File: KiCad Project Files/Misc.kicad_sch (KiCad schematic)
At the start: 19 parts, among them J2 SWD, U5 74AHCT1G125

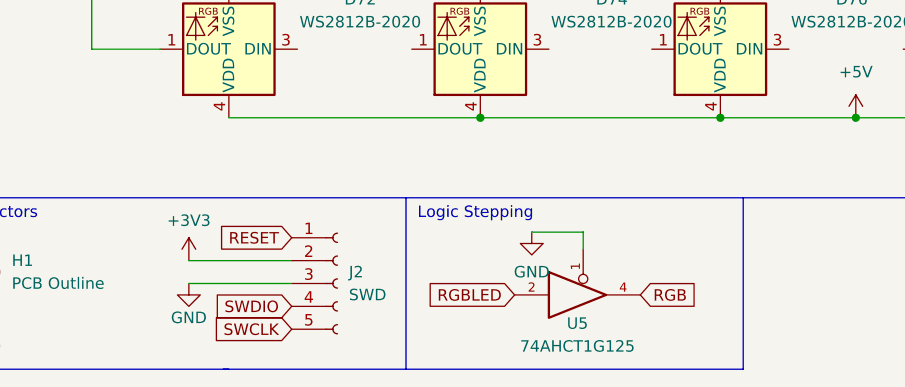
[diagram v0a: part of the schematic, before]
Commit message: begin work on stm32 branch
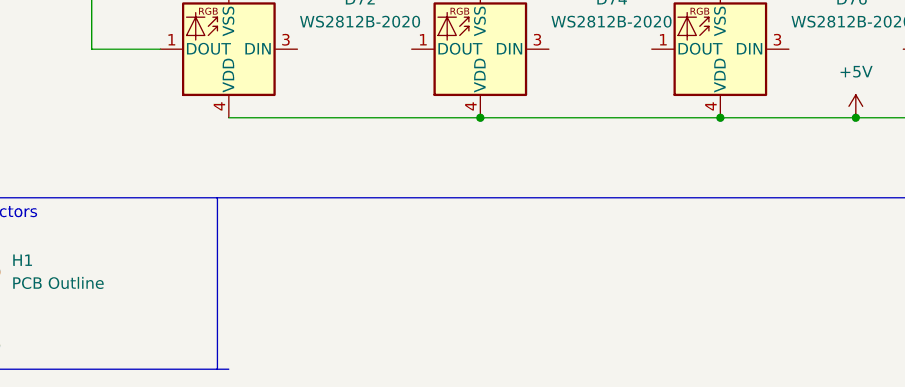
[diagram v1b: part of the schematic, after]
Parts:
- removed J2: SWD, Connector_PinHeader_2.54mm:PinHeader_1x05_P2.54mm_Vertical, symbol Connector:Conn_01x05_Female
- removed U5: 74AHCT1G125, Package_TO_SOT_SMD:SOT-23-5, symbol 74xGxx:74AHCT1G125
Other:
- note removed: "Logic Stepping"
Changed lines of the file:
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@@
-    (stroke (width 0) (type default) (color 0 0 0 0))
-  )
-  (wire (pts (xy 40.005 104.775) (xy 51.435 104.775))
     (stroke (width 0) (type default) (color 0 0 0 0))
   )
@@
     (stroke (width 0) (type default) (color 0 0 0 0))
   )
-  (polyline (pts (xy 101.6 114.3) (xy 101.6 95.25))
-    (stroke (width 0) (type default) (color 0 0 0 0))
-  )
-  (polyline (pts (xy 64.135 114.3) (xy 101.6 114.3))
-    (stroke (width 0) (type default) (color 0 0 0 0))
-  )
-  (wire (pts (xy 78.105 99.06) (xy 83.82 99.06))
+  (polyline (pts (xy 43.18 95.25) (xy 43.18 114.3))
     (stroke (width 0) (type default) (color 0 0 0 0))
   )
@@
     (stroke (width 0) (type default) (color 0 0 0 0))
   )
-  (wire (pts (xy 40.005 102.235) (xy 51.435 102.235))
-    (stroke (width 0) (type default) (color 0 0 0 0))
-  )
   (wire (pts (xy 44.45 19.685) (xy 71.755 19.685))
     (stroke (width 0) (type default) (color 0 0 0 0))
@@
     (stroke (width 0) (type default) (color 0 0 0 0))
   )
-  (polyline (pts (xy 43.815 114.3) (xy 64.135 114.3))
-    (stroke (width 0) (type default) (color 0 0 0 0))
-  )
-  (polyline (pts (xy 64.135 95.25) (xy 64.135 114.3))
-    (stroke (width 0) (type default) (color 0 0 0 0))
-  )
   (wire (pts (xy 133.985 27.305) (xy 146.05 27.305))
     (stroke (width 0) (type default) (color 0 0 0 0))
@@
     (stroke (width 0) (type default) (color 0 0 0 0))
   )
-  (wire (pts (xy 83.82 99.06) (xy 83.82 100.965))
-    (stroke (width 0) (type default) (color 0 0 0 0))
-  )
   (wire (pts (xy 71.755 19.685) (xy 99.06 19.685))
     (stroke (width 0) (type default) (color 0 0 0 0))
@@
   (polyline (pts (xy 222.25 95.25) (xy 12.7 95.25))
     (stroke (width 0) (type default) (color 0 0 0 0))
-  )
-  (text "Logic Stepping" (at 65.405 97.79 0)
-    (effects (font (size 1.27 1.27)) (justify left bottom))
   )
   (text "Connectors\n" (at 13.335 97.79 0)
@@
   (text "RGB\n" (at 13.335 15.24 0)
     (effects (font (size 1.27 1.27)) (justify left bottom))
-  )
-  (global_label "RGB" (shape input) (at 90.17 106.045 0) (fields_autoplaced)
-    (effects (font (size 1.27 1.27)) (justify left))
-    (property "Intersheet References" "${INTERSHEET_REFS}" (id 0) (at 96.3931 106.1244 0)
-      (effects (font (size 1.27 1.27)) (justify left) hide)
-    )
   )
   (global_label "RGB" (shape input) (at 36.83 27.305 180) (fields_autoplaced)
@@
     )
   )
-  (global_label "SWCLK" (shape input) (at 51.435 109.855 180) (fields_autoplaced)
-    (effects (font (size 1.27 1.27)) (justify right))
-    (property "Intersheet References" "${INTERSHEET_REFS}" (id 0) (at 42.7929 109.7756 0)
-      (effects (font (size 1.27 1.27)) (justify right) hide)
-    )
-  )
-  (global_label "RGBLED" (shape input) (at 76.2 106.045 180) (fields_autoplaced)
-    (effects (font (size 1.27 1.27)) (justify right))
-    (property "Intersheet References" "${INTERSHEET_REFS}" (id 0) (at 66.5298 105.9656 0)
-      (effects (font (size 1.27 1.27)) (justify right) hide)
-    )
-  )
-  (global_label "RESET" (shape input) (at 51.435 99.695 180) (fields_autoplaced)
-    (effects (font (size 1.27 1.27)) (justify right))
-    (property "Intersheet References" "${INTERSHEET_REFS}" (id 0) (at 43.2767 99.6156 0)
-      (effects (font (size 1.27 1.27)) (justify right) hide)
-    )
-  )
-  (global_label "SWDIO" (shape input) (at 51.435 107.315 180) (fields_autoplaced)
-    (effects (font (size 1.27 1.27)) (justify right))
-    (property "Intersheet References" "${INTERSHEET_REFS}" (id 0) (at 43.1557 107.2356 0)
-      (effects (font (size 1.27 1.27)) (justify right) hide)
-    )
-  )
   (symbol (lib_id "cipulot_parts:SK6812MINI") (at 29.21 43.18 90) (unit 1)
     (in_bom yes) (on_board yes) (fields_autoplaced)
@@
     (pin "4")
   )
-  (symbol (lib_id "74xGxx:74AHCT1G125") (at 83.82 106.045 0) (unit 1)
-    (in_bom yes) (on_board yes)
-    (property "Reference" "U5" (id 0) (at 83.185 109.22 0))
-    (property "Value" "74AHCT1G125" (id 1) (at 83.185 111.76 0))
-    (property "Footprint" "Package_TO_SOT_SMD:SOT-23-5" (id 2) (at 83.82 106.045 0)
-      (effects (font (size 1.27 1.27)) hide)
-    )
-    (property "Datasheet" "http://www.ti.com/lit/sg/scyt129e/scyt129e.pdf" (id 3) (at 85.09 117.475 0)
-      (effects (font (size 1.27 1.27)) hide)
-    )
-    (pin "1")
-    (pin "2")
-    (pin "3")
-    (pin "4")
-    (pin "5")
-  )
   (symbol (lib_id "power:GND") (at 17.145 107.315 0) (unit 1)
     (in_bom yes) (on_board yes) (fields_autoplaced)
@@
     (pin "1")
   )
-  (symbol (lib_id "power:GND") (at 40.005 104.775 0) (unit 1)
-    (in_bom yes) (on_board yes)
-    (property "Reference" "#PWR0139" (id 0) (at 40.005 111.125 0)
-      (effects (font (size 1.27 1.27)) hide)
-    )
-    (property "Value" "GND" (id 1) (at 40.005 108.585 0))
-    (property "Footprint" "" (id 2) (at 40.005 104.775 0)
-      (effects (font (size 1.27 1.27)) hide)
-    )
-    (property "Datasheet" "" (id 3) (at 40.005 104.775 0)
-      (effects (font (size 1.27 1.27)) hide)
-    )
-    (pin "1")
-  )
   (symbol (lib_id "cipulot_parts:SK6812MINI") (at 180.34 78.74 180) (unit 1)
     (in_bom yes) (on_board yes) (fields_autoplaced)
@@
   (symbol (lib_id "power:+5V") (at 205.105 52.07 0) (unit 1)
     (in_bom yes) (on_board yes) (fields_autoplaced)
-    (property "Reference" "#PWR?" (id 0) (at 205.105 55.88 0)
+    (property "Reference" "#PWR0113" (id 0) (at 205.105 55.88 0)
       (effects (font (size 1.27 1.27)) hide)
     )
@@
   (symbol (lib_id "power:+5V") (at 111.125 19.05 0) (unit 1)
     (in_bom yes) (on_board yes) (fields_autoplaced)
-    (property "Reference" "#PWR?" (id 0) (at 111.125 22.86 0)
+    (property "Reference" "#PWR0111" (id 0) (at 111.125 22.86 0)
       (effects (font (size 1.27 1.27)) hide)
     )
@@
   (symbol (lib_id "power:+5V") (at 114.113 86.36 0) (unit 1)
     (in_bom yes) (on_board yes) (fields_autoplaced)
-    (property "Reference" "#PWR?" (id 0) (at 114.113 90.17 0)
+    (property "Reference" "#PWR0112" (id 0) (at 114.113 90.17 0)
       (effects (font (size 1.27 1.27)) hide)
     )
@@
     (pin "4")
   )
-  (symbol (lib_id "power:GND") (at 78.105 99.06 0) (unit 1)
-    (in_bom yes) (on_board yes) (fields_autoplaced)
-    (property "Reference" "#PWR0145" (id 0) (at 78.105 105.41 0)
-      (effects (font (size 1.27 1.27)) hide)
-    )
-    (property "Value" "GND" (id 1) (at 78.105 103.505 0))
-    (property "Footprint" "" (id 2) (at 78.105 99.06 0)
-      (effects (font (size 1.27 1.27)) hide)
-    )
-    (property "Datasheet" "" (id 3) (at 78.105 99.06 0)
-      (effects (font (size 1.27 1.27)) hide)
-    )
-    (pin "1")
-  )
   (symbol (lib_id "cipulot_parts:SK6812MINI") (at 71.755 27.305 0) (unit 1)
     (in_bom yes) (on_board yes) (fields_autoplaced)
@@
   (symbol (lib_id "power:+5V") (at 20.32 52.07 0) (unit 1)
     (in_bom yes) (on_board yes) (fields_autoplaced)
-    (property "Reference" "#PWR?" (id 0) (at 20.32 55.88 0)
+    (property "Reference" "#PWR0114" (id 0) (at 20.32 55.88 0)
       (effects (font (size 1.27 1.27)) hide)
     )
@@
     )
     (pin "1")
-  )
-  (symbol (lib_id "Connector:Conn_01x05_Female") (at 56.515 104.775 0) (unit 1)
-    (in_bom yes) (on_board yes) (fields_autoplaced)
-    (property "Reference" "J2" (id 0) (at 57.785 103.5049 0)
-      (effects (font (size 1.27 1.27)) (justify left))
-    )
-    (property "Value" "SWD" (id 1) (at 57.785 106.0449 0)
-      (effects (font (size 1.27 1.27)) (justify left))
-    )
-    (property "Footprint" "Connector_PinHeader_2.54mm:PinHeader_1x05_P2.54mm_Vertical" (id 2) (at 56.515 104.775 0)
-      (effects (font (size 1.27 1.27)) hide)
-    )
-    (property "Datasheet" "~" (id 3) (at 56.515 104.775 0)
-      (effects (font (size 1.27 1.27)) hide)
-    )
-    (pin "1")
-    (pin "2")
-    (pin "3")
-    (pin "4")
-    (pin "5")
   )
   (symbol (lib_id "cipulot_parts:SK6812MINI") (at 195.58 43.18 270) (unit 1)
@@
     (pin "4")
   )
-  (symbol (lib_id "power:+3V3") (at 40.005 102.235 0) (unit 1)
-    (in_bom yes) (on_board yes)
-    (property "Reference" "#PWR0140" (id 0) (at 40.005 106.045 0)
-      (effects (font (size 1.27 1.27)) hide)
-    )
-    (property "Value" "+3V3" (id 1) (at 40.005 97.79 0))
-    (property "Footprint" "" (id 2) (at 40.005 102.235 0)
-      (effects (font (size 1.27 1.27)) hide)
-    )
-    (property "Datasheet" "" (id 3) (at 40.005 102.235 0)
-      (effects (font (size 1.27 1.27)) hide)
-    )
-    (pin "1")
-  )
   (symbol (lib_id "cipulot_parts:SK6812MINI") (at 153.67 78.74 180) (unit 1)
